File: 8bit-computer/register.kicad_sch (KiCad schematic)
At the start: 20 parts, among them U10 74LS173, U7 74LS245, U8 74LS173

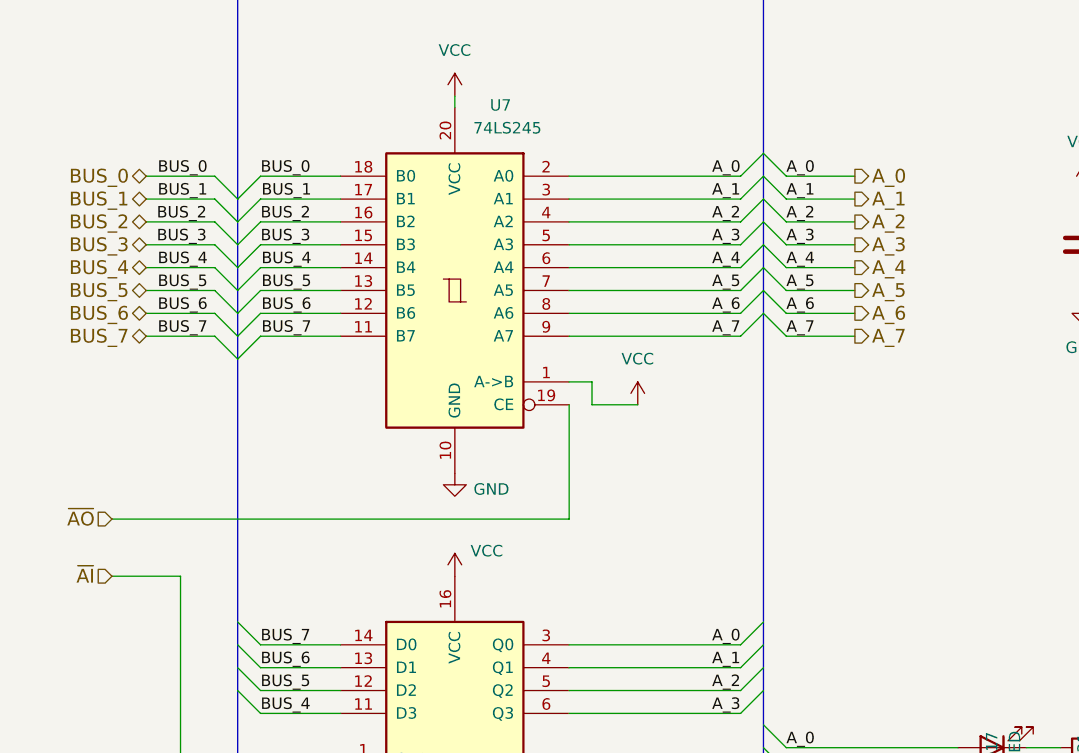
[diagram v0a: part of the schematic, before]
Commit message: using shared register schematic
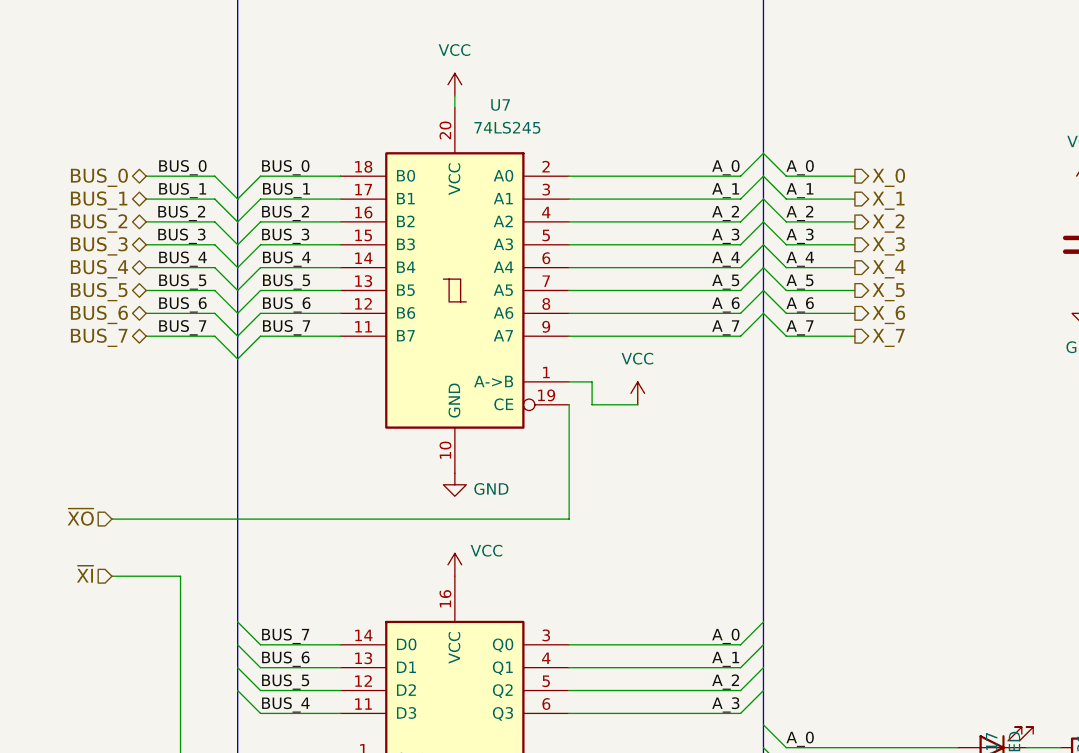
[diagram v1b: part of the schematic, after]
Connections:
- net A_0 renamed X_0
- net A_1 renamed X_1
- net A_2 renamed X_2
- net A_3 renamed X_3
- net A_4 renamed X_4
- net A_5 renamed X_5
- net A_6 renamed X_6
- net A_7 renamed X_7
- net ~{AI} renamed ~{XI}
- net ~{AO} renamed ~{XO}

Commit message: cont. 8bit schematics
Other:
- title: (none) -> Register (R)
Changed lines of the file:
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@@
 	(generator_version "10.0")
 	(paper "A4")
+	(title_block
+		(title "Register (R)")
+		(date "2026-05-15")
+	)
 	(junction
 		(at 143.51 135.89)
@@
 		(property "Reference" "R31"
 			(at 134.62 107.188 0)
+			(hide yes)
 			(show_name no)
 			(do_not_autoplace no)
@@
 		(property "Value" "220"
 			(at 137.16 107.188 0)
+			(hide yes)
 			(show_name no)
 			(do_not_autoplace no)
@@
 		(property "Reference" "R24"
 			(at 134.62 160.528 0)
+			(hide yes)
 			(show_name no)
 			(do_not_autoplace no)
@@
 		(property "Value" "220"
 			(at 137.16 160.528 0)
+			(hide yes)
 			(show_name no)
 			(do_not_autoplace no)
@@
 		(property "Reference" "D13"
 			(at 124.46 137.668 90)
+			(hide yes)
 			(show_name no)
 			(do_not_autoplace no)
@@
 		(property "Value" "RED"
 			(at 127 137.668 90)
+			(hide yes)
 			(show_name no)
 			(do_not_autoplace no)
@@
 		(property "Value" "GND"
 			(at 64.77 196.85 0)
+			(hide yes)
 			(show_name no)
 			(do_not_autoplace no)
@@
 		(property "Reference" "D17"
 			(at 124.46 107.188 90)
+			(hide yes)
 			(show_name no)
 			(do_not_autoplace no)
@@
 		(property "Value" "RED"
 			(at 127 107.188 90)
+			(hide yes)
 			(show_name no)
 			(do_not_autoplace no)
@@
 		(property "Value" "GND"
 			(at 49.53 114.3 0)
+			(hide yes)
 			(show_name no)
 			(do_not_autoplace no)
@@
 		(property "Reference" "D12"
 			(at 124.46 145.288 90)
+			(hide yes)
 			(show_name no)
 			(do_not_autoplace no)
@@
 		(property "Value" "RED"
 			(at 127 145.288 90)
+			(hide yes)
 			(show_name no)
 			(do_not_autoplace no)
@@
 		(property "Reference" "D14"
 			(at 124.46 130.048 90)
+			(hide yes)
 			(show_name no)
 			(do_not_autoplace no)
@@
 		(property "Value" "RED"
 			(at 127 130.048 90)
+			(hide yes)
 			(show_name no)
 			(do_not_autoplace no)
@@
 		(property "Value" "VCC"
 			(at 64.77 27.94 0)
+			(hide yes)
 			(show_name no)
 			(do_not_autoplace no)
@@
 		(property "Value" "GND"
 			(at 64.77 137.16 0)
+			(hide yes)
 			(show_name no)
 			(do_not_autoplace no)
@@
 		(property "Value" "GND"
 			(at 49.53 173.99 0)
+			(hide yes)
 			(show_name no)
 			(do_not_autoplace no)
@@
 		(property "Value" "GND"
 			(at 68.834 76.708 0)
+			(hide yes)
 			(show_name no)
 			(do_not_autoplace no)
@@
 		(property "Reference" "D11"
 			(at 124.46 152.908 90)
+			(hide yes)
 			(show_name no)
 			(do_not_autoplace no)
@@
 		(property "Value" "RED"
 			(at 127 152.908 90)
+			(hide yes)
 			(show_name no)
 			(do_not_autoplace no)
@@
 		(property "Reference" "R26"
 			(at 134.62 145.288 0)
+			(hide yes)
 			(show_name no)
 			(do_not_autoplace no)
@@
 		(property "Value" "220"
 			(at 137.16 145.288 0)
+			(hide yes)
 			(show_name no)
 			(do_not_autoplace no)
@@
 		(property "Reference" "D16"
 			(at 124.46 114.808 90)
+			(hide yes)
 			(show_name no)
 			(do_not_autoplace no)
@@
 		(property "Value" "RED"
 			(at 127 114.808 90)
+			(hide yes)
 			(show_name no)
 			(do_not_autoplace no)
@@
 		(property "Reference" "R25"
 			(at 134.62 152.908 0)
+			(hide yes)
 			(show_name no)
 			(do_not_autoplace no)
@@
 		(property "Value" "220"
 			(at 137.16 152.908 0)
+			(hide yes)
 			(show_name no)
 			(do_not_autoplace no)
@@
 		(property "Value" "VCC"
 			(at 85.09 62.23 0)
+			(hide yes)
 			(show_name no)
 			(do_not_autoplace no)
@@
 		(property "Reference" "R29"
 			(at 134.62 122.428 0)
+			(hide yes)
 			(show_name no)
 			(do_not_autoplace no)
@@
 		(property "Value" "220"
 			(at 137.16 122.428 0)
+			(hide yes)
 			(show_name no)
 			(do_not_autoplace no)
@@
 		(property "Reference" "R28"
 			(at 134.62 130.048 0)
+			(hide yes)
 			(show_name no)
 			(do_not_autoplace no)
@@
 		(property "Value" "220"
 			(at 137.16 130.048 0)
+			(hide yes)
 			(show_name no)
 			(do_not_autoplace no)
@@
 		(property "Value" "GND"
 			(at 148.59 137.16 0)
+			(hide yes)
 			(show_name no)
 			(do_not_autoplace no)
@@
 		(property "Reference" "R27"
 			(at 134.62 137.668 0)
+			(hide yes)
 			(show_name no)
 			(do_not_autoplace no)
@@
 		(property "Value" "220"
 			(at 137.16 137.668 0)
+			(hide yes)
 			(show_name no)
 			(do_not_autoplace no)
@@
 		(property "Reference" "D15"
 			(at 124.46 122.428 90)
+			(hide yes)
 			(show_name no)
 			(do_not_autoplace no)
@@
 		(property "Value" "RED"
 			(at 127 122.428 90)
+			(hide yes)
 			(show_name no)
 			(do_not_autoplace no)
@@
 		(property "Value" "VCC"
 			(at 68.326 83.566 0)
+			(hide yes)
 			(show_name no)
 			(do_not_autoplace no)
@@
 		(property "Value" "VCC"
 			(at 64.77 140.97 0)
+			(hide yes)
 			(show_name no)
 			(do_not_autoplace no)
@@
 		(property "Reference" "D10"
 			(at 124.46 160.528 90)
+			(hide yes)
 			(show_name no)
 			(do_not_autoplace no)
@@
 		(property "Value" "RED"
 			(at 127 160.528 90)
+			(hide yes)
 			(show_name no)
 			(do_not_autoplace no)
@@
 		(property "Reference" "R30"
 			(at 134.62 114.808 0)
+			(hide yes)
 			(show_name no)
 			(do_not_autoplace no)
@@
 		(property "Value" "220"
 			(at 137.16 114.808 0)
+			(hide yes)
 			(show_name no)
 			(do_not_autoplace no)
@@
 		)
 	)
-	(sheet_instances
-		(path "/"
-			(page "1")
-		)
-	)
